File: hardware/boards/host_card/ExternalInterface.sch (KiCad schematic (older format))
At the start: 4 parts, among them U1 ECP5UM5G-381caBGA, X1 AX3

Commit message: Fixed  / updated the ECP5 symbol for the ECP5UM5G-85K
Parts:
- U1: symbol lethalbit:ECP5UM5G-381caBGA -> lethalbit:LFE5UM5G-85F-8BG381I
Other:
- moved on the sheet: C59, R56, X1
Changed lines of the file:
@@
 Comment4 ""
 $EndDescr
-NoConn ~ 4650 3200
-NoConn ~ 4650 3300
-NoConn ~ 4650 3400
-NoConn ~ 4650 3500
-NoConn ~ 4650 3600
-NoConn ~ 4650 3700
-NoConn ~ 4650 3800
-NoConn ~ 4650 3900
-NoConn ~ 4650 4000
-NoConn ~ 4650 4100
-NoConn ~ 4650 4200
-NoConn ~ 4650 4300
-NoConn ~ 4650 4400
-NoConn ~ 4650 4500
-NoConn ~ 6150 4200
-NoConn ~ 6150 4100
-NoConn ~ 6150 4000
-NoConn ~ 6150 3900
-NoConn ~ 6150 3800
-NoConn ~ 6150 3700
-NoConn ~ 6150 3600
-NoConn ~ 6150 3500
-NoConn ~ 6150 3400
-NoConn ~ 6150 3300
-NoConn ~ 6150 3200
+NoConn ~ 4950 3200
+NoConn ~ 4950 3300
+NoConn ~ 4950 3400
+NoConn ~ 4950 3500
+NoConn ~ 4950 3600
+NoConn ~ 4950 3700
+NoConn ~ 4950 3800
+NoConn ~ 4950 3900
+NoConn ~ 4950 4000
+NoConn ~ 4950 4100
+NoConn ~ 4950 4200
+NoConn ~ 4950 4300
+NoConn ~ 4950 4400
+NoConn ~ 4950 4500
+NoConn ~ 5850 4200
+NoConn ~ 5850 4100
+NoConn ~ 5850 4000
+NoConn ~ 5850 3900
+NoConn ~ 5850 3800
+NoConn ~ 5850 3700
+NoConn ~ 5850 3600
+NoConn ~ 5850 3500
+NoConn ~ 5850 3400
+NoConn ~ 5850 3300
+NoConn ~ 5850 3200
 $Comp
-L lethalbit:ECP5UM5G-381caBGA U?
+L lethalbit:LFE5UM5G-85F-8BG381I U?
 U 2 1 5FD7F3DB
 P 5400 3250
 AR Path="/5EDAB834/5FD7F3DB" Ref="U?"  Part="2"
 AR Path="/5EF6A128/5FD7F3DB" Ref="U1"  Part="2"
+AR Path="/5FD7F3DB" Ref="U1"  Part="2"
 F 0 "U1" H 5400 3598 50  0000 C CNN
 F 1 "ECP5UM5G-381caBGA" H 5400 3507 50  0000 C CNN
@@
 L lethalbit:AX3 X?
 U 1 1 5FDEF1C0
-P 7300 4450
+P 7000 4450
 AR Path="/5EDAB834/5FDEF1C0" Ref="X?"  Part="1"
 AR Path="/5EF6A128/5FDEF1C0" Ref="X1"  Part="1"
-F 0 "X1" H 7300 4825 50  0000 C CNN
-F 1 "AX3" H 7300 4734 50  0000 C CNN
-F 2 "lethalbit:AX3" H 6950 4750 50  0001 C CNN
-F 3 "https://abracon.com/datasheets/AX3.pdf" H 6950 4750 50  0001 C CNN
-F 4 "Abracon LLC" H 7300 4450 50  0001 C CNN "MFR"
-F 5 "AX3DCF1-100.0000" H 7300 4450 50  0001 C CNN "MPN"
-	1    7300 4450
+F 0 "X1" H 7000 4825 50  0000 C CNN
+F 1 "AX3" H 7000 4734 50  0000 C CNN
+F 2 "lethalbit:AX3" H 6650 4750 50  0001 C CNN
+F 3 "https://abracon.com/datasheets/AX3.pdf" H 6650 4750 50  0001 C CNN
+F 4 "Abracon LLC" H 7000 4450 50  0001 C CNN "MFR"
+F 5 "AX3DCF1-100.0000" H 7000 4450 50  0001 C CNN "MPN"
+	1    7000 4450
 	-1   0    0    -1
 $EndComp
@@
 L Device:R_Small R?
 U 1 1 5FDEF1C8
-P 6550 4350
+P 6250 4350
 AR Path="/5EDAB834/5FDEF1C8" Ref="R?"  Part="1"
 AR Path="/5EF6A128/5FDEF1C8" Ref="R56"  Part="1"
-F 0 "R56" V 6450 4300 50  0000 L CNN
-F 1 "100" V 6650 4250 50  0000 L CNN
-F 2 "Resistor_SMD:R_0402_1005Metric" H 6550 4350 50  0001 C CNN
-F 3 "~" H 6550 4350 50  0001 C CNN
-F 4 "Vishay Dale" H 6550 4350 50  0001 C CNN "MFR"
-F 5 "RCS0402100RFKED" V 6550 4350 50  0001 C CNN "MPN"
-	1    6550 4350
+F 0 "R56" V 6150 4300 50  0000 L CNN
+F 1 "100" V 6350 4250 50  0000 L CNN
+F 2 "Resistor_SMD:R_0402_1005Metric" H 6250 4350 50  0001 C CNN
+F 3 "~" H 6250 4350 50  0001 C CNN
+F 4 "Vishay Dale" H 6250 4350 50  0001 C CNN "MFR"
+F 5 "RCS0402100RFKED" V 6250 4350 50  0001 C CNN "MPN"
+	1    6250 4350
 	1    0    0    -1
 $EndComp
 Wire Wire Line
-	6150 4400 6400 4400
+	5850 4400 6100 4400
 Wire Wire Line
-	6400 4400 6400 4500
+	6100 4400 6100 4500
 Wire Wire Line
-	6400 4500 6550 4500
+	6100 4500 6250 4500
 Wire Wire Line
-	6700 4500 6700 4400
+	6400 4500 6400 4400
 Wire Wire Line
-	6700 4400 7000 4400
+	6400 4400 6700 4400
 Wire Wire Line
-	7000 4300 6700 4300
+	6700 4300 6400 4300
 Wire Wire Line
-	6700 4300 6700 4200
+	6400 4300 6400 4200
 Wire Wire Line
-	6700 4200 6550 4200
+	6400 4200 6250 4200
 Wire Wire Line
-	6400 4200 6400 4300
+	6100 4200 6100 4300
 Wire Wire Line
-	6400 4300 6150 4300
+	6100 4300 5850 4300
 Wire Wire Line
-	6550 4200 6550 4250
-Connection ~ 6550 4200
+	6250 4200 6250 4250
+Connection ~ 6250 4200
 Wire Wire Line
-	6550 4200 6400 4200
+	6250 4200 6100 4200
 Wire Wire Line
-	6550 4450 6550 4500
-Connection ~ 6550 4500
+	6250 4450 6250 4500
+Connection ~ 6250 4500
 Wire Wire Line
-	6550 4500 6700 4500
+	6250 4500 6400 4500
 $Comp
 L power:GND #PWR?
 U 1 1 5FDEF1DE
-P 7700 4750
+P 7400 4750
 AR Path="/5EDAB834/5FDEF1DE" Ref="#PWR?"  Part="1"
 AR Path="/5EF6A128/5FDEF1DE" Ref="#PWR0139"  Part="1"
-F 0 "#PWR0139" H 7700 4500 50  0001 C CNN
-F 1 "GND" H 7705 4577 50  0000 C CNN
-F 2 "" H 7700 4750 50  0001 C CNN
-F 3 "" H 7700 4750 50  0001 C CNN
-	1    7700 4750
+F 0 "#PWR0139" H 7400 4500 50  0001 C CNN
+F 1 "GND" H 7405 4577 50  0000 C CNN
+F 2 "" H 7400 4750 50  0001 C CNN
+F 3 "" H 7400 4750 50  0001 C CNN
+	1    7400 4750
 	1    0    0    -1
 $EndComp
 Wire Wire Line
-	7600 4600 7700 4600
+	7300 4600 7400 4600
 Wire Wire Line
-	7700 4600 7700 4750
+	7400 4600 7400 4750
 $Comp
 L Device:C_Small C?
 U 1 1 5FDEF1E8
-P 7950 4550
+P 7650 4550
 AR Path="/5EDF9F51/5FDEF1E8" Ref="C?"  Part="1"
 AR Path="/5EDAB834/5FDEF1E8" Ref="C?"  Part="1"
 AR Path="/5EF6A128/5FDEF1E8" Ref="C59"  Part="1"
-F 0 "C59" H 7858 4504 50  0000 R CNN
-F 1 "0.1uF" H 7858 4595 50  0000 R CNN
-F 2 "Capacitor_SMD:C_0603_1608Metric" H 7950 4550 50  0001 C CNN
-F 3 "~" H 7950 4550 50  0001 C CNN
-F 4 "KEMET" V 7950 4550 50  0001 C CNN "MFR"
-F 5 "C0603C104M5RACTU" V 7950 4550 50  0001 C CNN "MPN"
-	1    7950 4550
+F 0 "C59" H 7558 4504 50  0000 R CNN
+F 1 "0.1uF" H 7558 4595 50  0000 R CNN
+F 2 "Capacitor_SMD:C_0603_1608Metric" H 7650 4550 50  0001 C CNN
+F 3 "~" H 7650 4550 50  0001 C CNN
+F 4 "KEMET" V 7650 4550 50  0001 C CNN "MFR"
+F 5 "C0603C104M5RACTU" V 7650 4550 50  0001 C CNN "MPN"
+	1    7650 4550
 	-1   0    0    1
 $EndComp
 Wire Wire Line
-	7700 4600 7800 4600
+	7400 4600 7500 4600
 Wire Wire Line
-	7800 4600 7800 4700
+	7500 4600 7500 4700
 Wire Wire Line
-	7800 4700 7950 4700
+	7500 4700 7650 4700
 Wire Wire Line
-	7950 4700 7950 4650
-Connection ~ 7700 4600
+	7650 4700 7650 4650
+Connection ~ 7400 4600
 Wire Wire Line
-	7600 4500 7800 4500
+	7300 4500 7500 4500
 Wire Wire Line
-	7800 4500 7800 4400
+	7500 4500 7500 4400
 Wire Wire Line
-	7800 4400 7950 4400
+	7500 4400 7650 4400
 Wire Wire Line
-	7950 4400 7950 4450
+	7650 4400 7650 4450
 Wire Wire Line
-	7600 4300 7800 4300
+	7300 4300 7500 4300
 Wire Wire Line
-	7800 4300 7800 4400
-Connection ~ 7800 4400
+	7500 4300 7500 4400
+Connection ~ 7500 4400
 Wire Wire Line
-	7800 4300 8050 4300
-Connection ~ 7800 4300
-Text Label 8050 4300 2    50   ~ 0
+	7500 4300 7750 4300
+Connection ~ 7500 4300
+Text Label 7750 4300 2    50   ~ 0
 _1V8
-Text Label 6700 4300 0    50   ~ 0
+Text Label 6400 4300 0    50   ~ 0
 CLK+
-Text Label 6700 4400 0    50   ~ 0
+Text Label 6400 4400 0    50   ~ 0
 CLK-
 Text HLabel 750  700  0    39   Input ~ 0

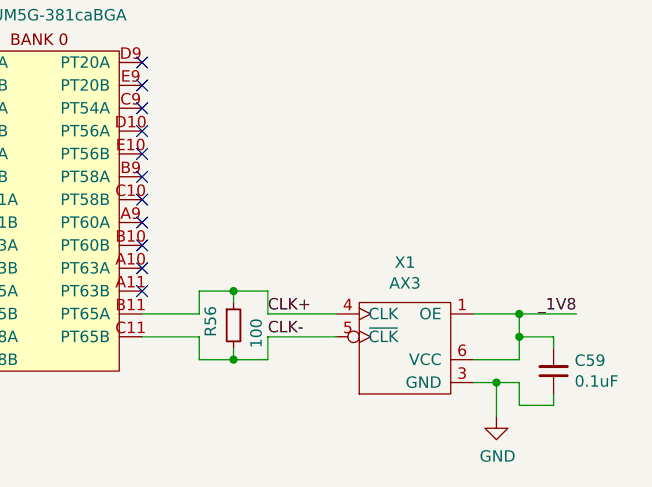
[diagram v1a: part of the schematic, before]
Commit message: Broke out the DDR3 modules and added the 0.75V LDO for the VREFCA and VREFDQ lines for each of the DDR3 modules
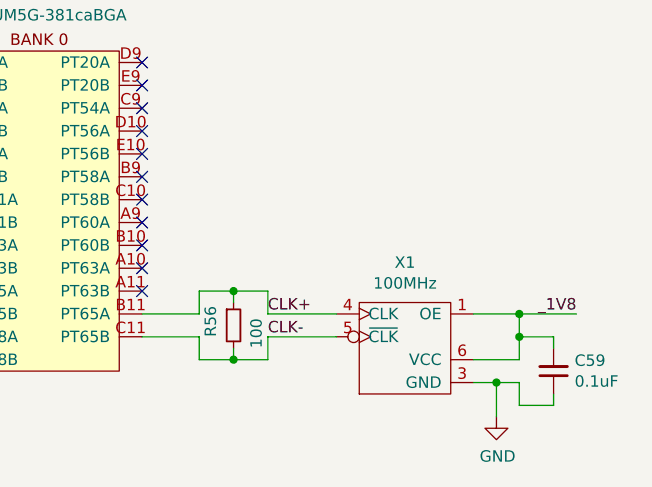
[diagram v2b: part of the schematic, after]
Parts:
- X1: value AX3 -> 100MHz
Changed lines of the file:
@@
 AR Path="/5EF6A128/5FDEF1C0" Ref="X1"  Part="1"
 F 0 "X1" H 7000 4825 50  0000 C CNN
-F 1 "AX3" H 7000 4734 50  0000 C CNN
+F 1 "100MHz" H 7000 4734 50  0000 C CNN
 F 2 "lethalbit:AX3" H 6650 4750 50  0001 C CNN
 F 3 "https://abracon.com/datasheets/AX3.pdf" H 6650 4750 50  0001 C CNN
